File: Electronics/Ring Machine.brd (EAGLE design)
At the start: 19 parts, among them IC1 REG1117, U3 LM3480-3.3, X1 22-23-2081, X2 22-23-2081

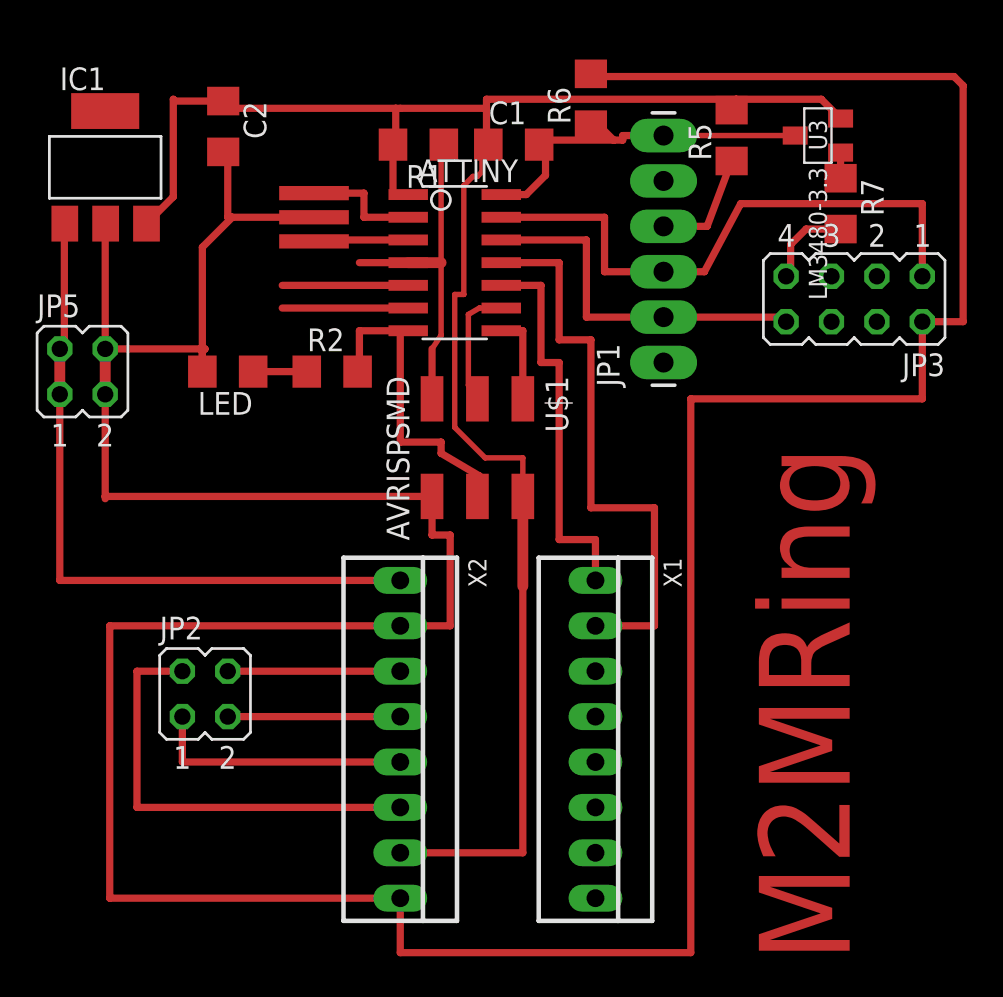
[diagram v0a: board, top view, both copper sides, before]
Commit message: 5v regulator electronics
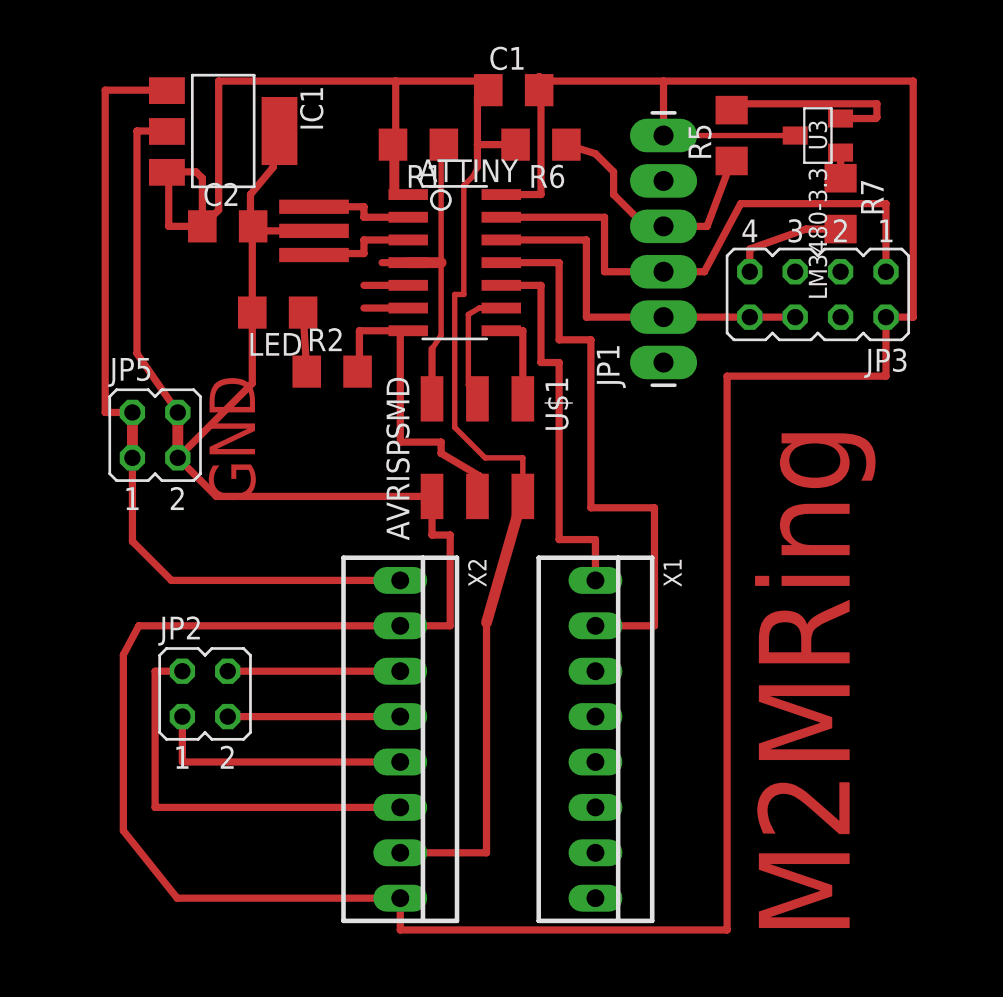
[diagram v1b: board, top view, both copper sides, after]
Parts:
- moved IC1 6.91 mm to (17.5, 56.6), turned to 270 degrees
- moved C2 5.59 mm to (17.8, 51.3), turned to 0 degrees
- moved JP5 5.40 mm to (13.7, 39.6)
- moved LED 4.33 mm to (20.6, 46.5)
- moved R6 3.78 mm to (35.3, 55.9), turned to 180 degrees
- moved C1 3.05 mm to (33.8, 58.9)
- moved JP3 2.05 mm to (50.8, 47.5)
- moved QUARTZ 0.76 mm to (22.6, 51.1)
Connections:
- net GND: no longer R6.1, R6.2
- net VCC: now also R6.1, R6.2
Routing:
- net VCC: track 111.6 -> 122.8 mm
- net GND: track 243.6 -> 234.5 mm
- net VBB: track 39.7 -> 46.1 mm
- net IN2B: track 7.05 -> 2.48 mm
- net IN1B: track 7.05 -> 2.48 mm
- net TX: track 33.0 -> 30.7 mm
- net 1B: track 24.9 -> 22.9 mm
- net VCCESP: track 6.47 -> 7.98 mm
- net N$1: track 2.29 -> 1.02 mm
- net XTAL1: track 6.62 -> 5.86 mm
- net XTAL2: track 5.35 -> 6.04 mm
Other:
- board text added: "GND"
